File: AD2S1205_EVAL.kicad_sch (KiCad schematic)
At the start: 8 parts, among them U1 AD2S1205, Y1 Crystal

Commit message: Driver schematic done
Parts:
- added C4: 100n, Capacitor_SMD:C_0805_2012Metric_Pad1.18x1.45mm_HandSolder, symbol Device:C
- added C5, C9: 1u, Capacitor_SMD:C_0805_2012Metric_Pad1.18x1.45mm_HandSolder, symbol Device:C
- added C6, C8: DNP, Capacitor_SMD:C_0805_2012Metric_Pad1.18x1.45mm_HandSolder, symbol Device:C
- added C7: C, Capacitor_SMD:C_0805_2012Metric_Pad1.18x1.45mm_HandSolder, symbol Device:C
- added D1, D2, D3, D4: 1N4148, Diode_THT:D_DO-35_SOD27_P7.62mm_Horizontal, symbol Diode:1N4148
- added J1: SIN, Connector_PinHeader_2.54mm:PinHeader_1x02_P2.54mm_Vertical, symbol Connector:Conn_01x02_Pin
- added J2: Power, Connector_PinHeader_2.54mm:PinHeader_1x03_P2.54mm_Vertical, symbol Connector:Conn_01x03_Pin
- added J3: Interface, Connector_PinHeader_2.54mm:PinHeader_1x06_P2.54mm_Vertical, symbol Connector:Conn_01x06_Pin
- added J4: COS, Connector_PinHeader_2.54mm:PinHeader_1x02_P2.54mm_Vertical, symbol Connector:Conn_01x02_Pin
- added J5: DEBUG, symbol Connector:Conn_01x07_Pin
- added Q1, Q3: BD135, Package_TO_SOT_THT:TO-126-3_Vertical, symbol Transistor_BJT:BD135
- added Q2, Q4: BD136, Package_TO_SOT_THT:TO-126-3_Vertical, symbol Transistor_BJT:BD136
- added R10, R11: 22k, Resistor_SMD:R_0805_2012Metric, symbol Device:R
- added R12, R13, R5, R7: 2.2k, Resistor_SMD:R_0805_2012Metric, symbol Device:R
- added R4, R6, R8, R9: 10k, Resistor_SMD:R_0805_2012Metric, symbol Device:R
- added U2: LM358, Package_SO:SO-8_3.9x4.9mm_P1.27mm, symbol Amplifier_Operational:LM358
- C1: footprint (none) -> Capacitor_SMD:C_0805_2012Metric_Pad1.18x1.45mm_HandSolder
- C2, C3: value C -> DNP; footprint (none) -> Capacitor_SMD:C_0805_2012Metric_Pad1.18x1.45mm_HandSolder
- R1, R2: value R -> 68k; footprint (none) -> Resistor_SMD:R_0805_2012Metric
- R3: footprint (none) -> Resistor_SMD:R_0805_2012Metric
- Y1: footprint (none) -> Crystal:Crystal_HC49-U_Vertical
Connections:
- net +5V: now also U1.1 (DVDD), U1.17 (DVDD), U1.39 (AVdd), C4.1, C5.1, C9.1, R10.2
- net GND: now also U1.3 (~{CS}), U1.6 (~{SOE}), C4.2, C5.2, C7.2, C9.2, J3.6 (Pin_6), J5.7 (Pin_7), Q2.1 (E), Q4.1 (E), R11.1, R13.2, R7.2, U2.4 (V-)
- net ~{RD}: now reaches U1.2 (~{RD})
- net ~{RD}: now also J3.1 (Pin_1)
- net at U1.25 (A): now also J5.1 (Pin_1)
- net at U1.26 (B): now also J5.2 (Pin_2)
- net at U1.27 (NM): now also J5.3 (Pin_3)
- net at U1.28 (DIR): now also J5.4 (Pin_4)
- net at U1.29 (DOS): now also J5.5 (Pin_5)
- net at U1.30 (LOT): now also J5.6 (Pin_6)
- net EXC: now reaches U1.34 (EXC)
- net EXC: now also R9.1
- net ~{EXC}: now reaches U1.35 (~{EXC})
- net ~{EXC}: now also R4.1
- net at R1.1, U1.37 (Sin): now also J1.2 (Pin_2)
- net at R1.2, U1.38 (SinLO): now also J1.1 (Pin_1)
- net ~{SAMPLE}: now reaches U1.4 (~{SAMPLE})
- net ~{SAMPLE}: now also J3.2 (Pin_2)
- net at R2.1, U1.40 (CosLO): now also J4.2 (Pin_2)
- net at R2.2, U1.41 (Cos): now also J4.1 (Pin_1)
- net ~{RDVEL}: now reaches U1.5 (~{RDVEL})
- net ~{RDVEL}: now also J3.3 (Pin_3)
- net SO: now reaches U1.7 (DB11/SO)
- net SO: now also J3.5 (Pin_5)
- net SCLK: now reaches U1.8 (DB10)
- net SCLK: now also J3.4 (Pin_4)
- new net: D2.2 (A), Q1.3 (B), R5.2
- new net: D4.1 (K), Q4.3 (B), R13.1
- new net: D3.1 (K), D4.2 (A), U2.1
- new net: D3.2 (A), Q3.3 (B), R12.2
- new net: C8.1, R4.2, R6.1, U2.2 (-)
- new net: C8.2, Q3.1 (E), Q4.2 (C), R6.2
- new net: D1.1 (K), Q2.3 (B), R7.1
- new net: D1.2 (A), D2.1 (K), U2.7
- new net: C6.2, Q1.1 (E), Q2.2 (C), R8.2
- new net: C6.1, R8.1, R9.2, U2.6 (-)
- new net +12V: C7.1, Q1.2 (C), Q3.2 (C), R12.1, R5.1, U2.8 (V+)
- new net 2.5V: R10.1, R11.2, U2.3 (+), U2.5 (+)
- no-connect marks 0 -> 14
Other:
- moved on the sheet: C1, R1, R2, R3

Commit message: Layout
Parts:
- added J6: EXC, Connector_PinHeader_2.54mm:PinHeader_1x02_P2.54mm_Vertical, symbol Connector:Conn_01x02_Pin
- C1: value C -> 1u
- C7: value C -> 100n
- D1, D2, D3, D4: footprint Diode_THT:D_DO-35_SOD27_P7.62mm_Horizontal -> Diode_SMD:D_SMA_Handsoldering
- J5: footprint (none) -> Connector_PinHeader_2.54mm:PinHeader_1x07_P2.54mm_Vertical
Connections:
- net +12V: now also J2.1 (Pin_1)
- net +5V: now also J2.2 (Pin_2)
- net GND: now also J2.3 (Pin_3), J3.4 (Pin_4), Q2.2 (C), Q4.2 (C); no longer J3.6 (Pin_6), Q2.1 (E), Q4.1 (E)
- net SCLK: now also J3.6 (Pin_6); no longer J3.4 (Pin_4)
- net ~{EXC_AMP}: now reaches C8.2, Q3.1 (E), R6.2
- net ~{EXC_AMP}: now also Q4.1 (E), J6.1 (Pin_1); no longer Q4.2 (C)
- net EXC_AMP: now reaches C6.2, Q1.1 (E), R8.2
- net EXC_AMP: now also Q2.1 (E), J6.2 (Pin_2); no longer Q2.2 (C)
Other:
- moved on the sheet: J2

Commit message: layout complete
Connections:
- net +5V: now also J2.3 (Pin_3); no longer J2.2 (Pin_2)
- net GND: now also J2.2 (Pin_2); no longer J2.3 (Pin_3)
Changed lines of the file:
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@@
+    (stroke (width 0) (type default))
+  )
+  (wire (pts (xy 22.86 24.13) (xy 30.48 24.13))
     (stroke (width 0) (type default))
   )
@@
     (stroke (width 0) (type default))
   )
+  (wire (pts (xy 22.86 21.59) (xy 25.4 21.59))
+    (stroke (width 0) (type default))
+  )
   (wire (pts (xy 215.9 60.96) (xy 218.44 60.96))
     (stroke (width 0) (type default))
@@
     (stroke (width 0) (type default))
   )
-  (wire (pts (xy 25.4 24.13) (xy 22.86 24.13))
-    (stroke (width 0) (type default))
-  )
   (wire (pts (xy 218.44 60.96) (xy 223.52 60.96))
     (stroke (width 0) (type default))
@@
     (stroke (width 0) (type default))
   )
-  (wire (pts (xy 25.4 26.67) (xy 25.4 24.13))
+  (wire (pts (xy 25.4 21.59) (xy 25.4 26.67))
     (stroke (width 0) (type default))
   )
@@
   )
   (wire (pts (xy 257.81 38.1) (xy 257.81 45.72))
-    (stroke (width 0) (type default))
-  )
-  (wire (pts (xy 30.48 21.59) (xy 22.86 21.59))
     (stroke (width 0) (type default))
   )
@@
     )
   )
-  (symbol (lib_id "power:+5V") (at 30.48 21.59 0) (unit 1)
-    (in_bom yes) (on_board yes) (dnp no) (fields_autoplaced)
-    (property "Reference" "#PWR025" (at 30.48 25.4 0)
-      (effects (font (size 1.27 1.27)) hide)
-    )
-    (property "Value" "+5V" (at 30.48 17.78 0)
-      (effects (font (size 1.27 1.27)))
-    )
-    (property "Footprint" "" (at 30.48 21.59 0)
-      (effects (font (size 1.27 1.27)) hide)
-    )
-    (property "Datasheet" "" (at 30.48 21.59 0)
-      (effects (font (size 1.27 1.27)) hide)
-    )
+  (symbol (lib_id "power:+5V") (at 30.48 24.13 0) (unit 1)
+    (in_bom yes) (on_board yes) (dnp no) (fields_autoplaced)
+    (property "Reference" "#PWR025" (at 30.48 27.94 0)
+      (effects (font (size 1.27 1.27)) hide)
+    )
+    (property "Value" "+5V" (at 30.48 20.32 0)
+      (effects (font (size 1.27 1.27)))
+    )
+    (property "Footprint" "" (at 30.48 24.13 0)
+      (effects (font (size 1.27 1.27)) hide)
+    )
+    (property "Datasheet" "" (at 30.48 24.13 0)
+      (effects (font (size 1.27 1.27)) hide)
+    )

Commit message: layout complete
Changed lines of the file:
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@@
-    (stroke (width 0) (type default))
-  )
-  (wire (pts (xy 44.45 104.14) (xy 46.99 104.14))
     (stroke (width 0) (type default))
   )

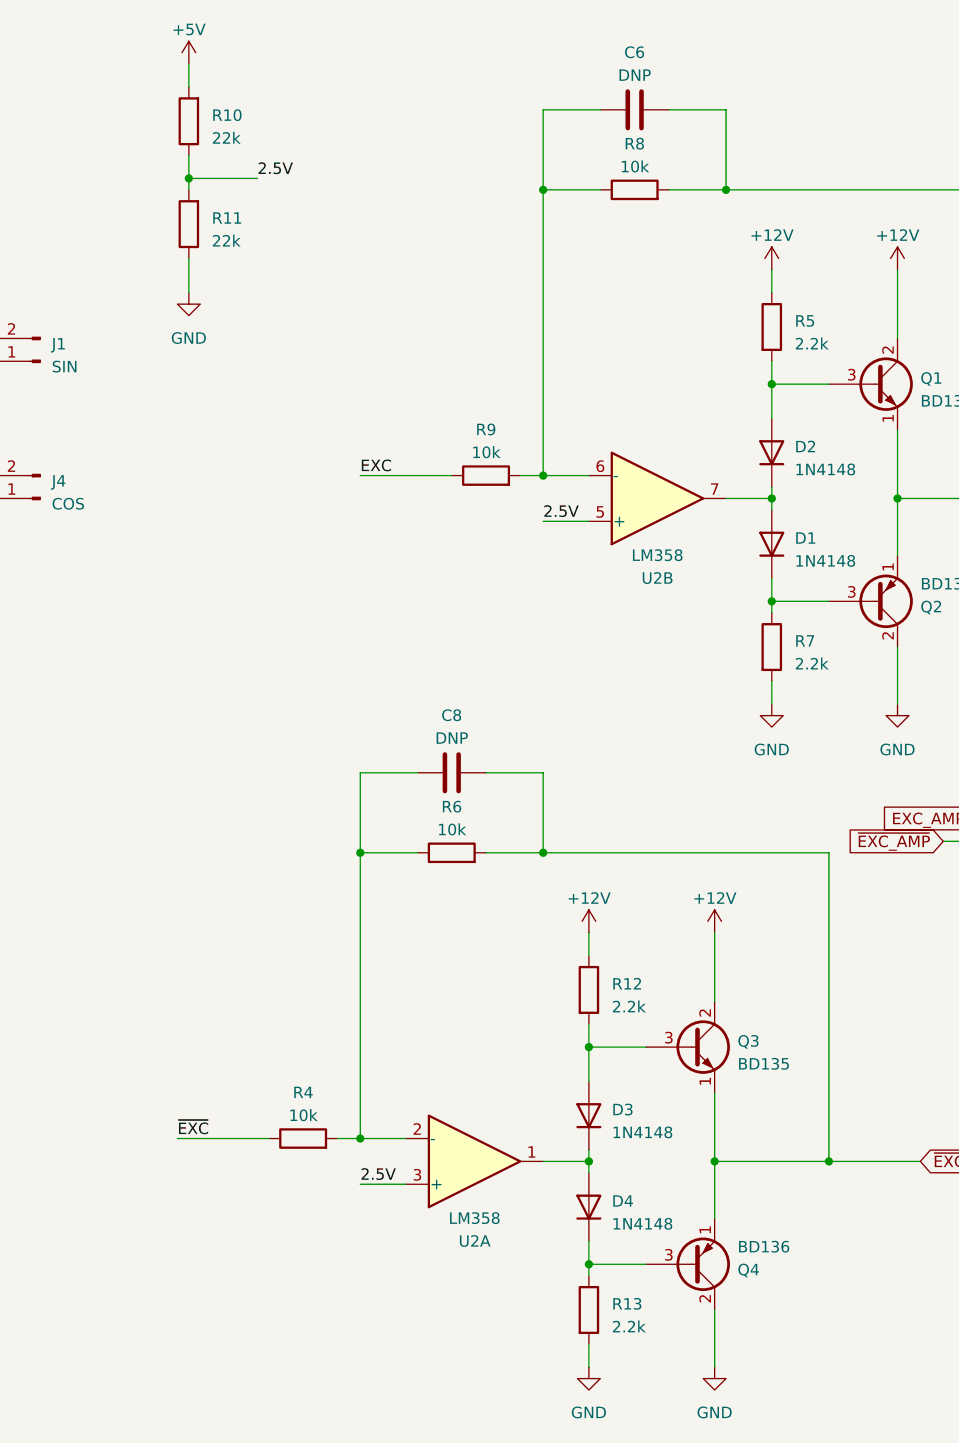
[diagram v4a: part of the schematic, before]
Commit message: Middle point repaired, added crossover dist resistors
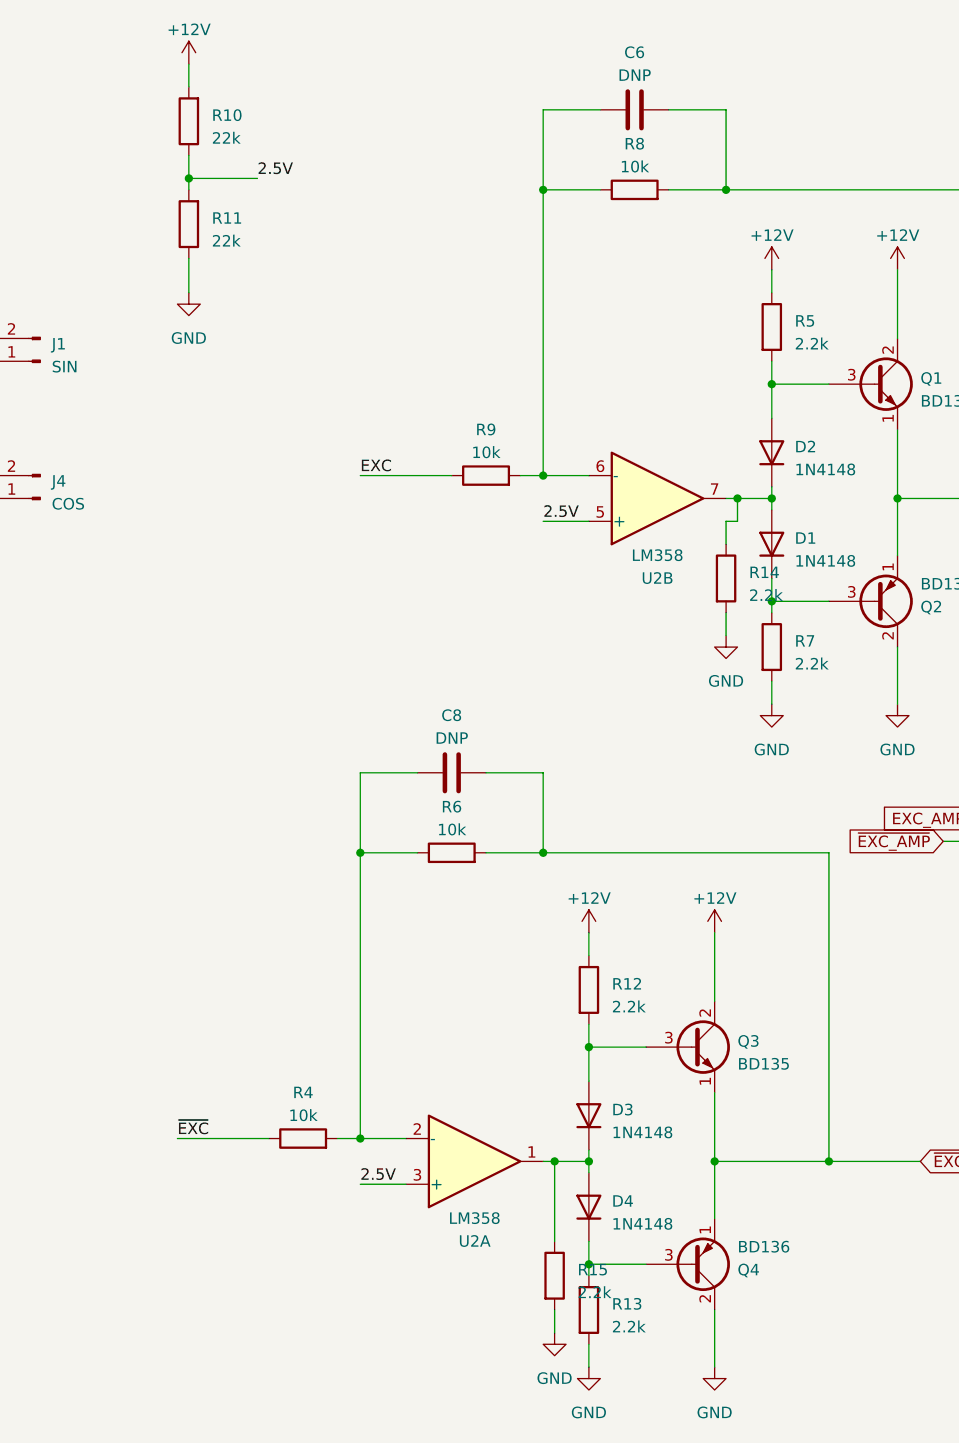
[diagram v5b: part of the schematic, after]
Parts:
- added R14, R15: 2.2k, Resistor_SMD:R_0805_2012Metric, symbol Device:R
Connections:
- net +12V: now also R10.2
- net +5V: no longer R10.2
- net GND: now also R14.2, R15.2
- net at D3.1 (K), D4.2 (A), U2.1: now also R15.1
- net at D1.2 (A), D2.1 (K), U2.7: now also R14.1
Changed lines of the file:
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@@
   (junction (at 223.52 137.16) (diameter 0) (color 0 0 0 0)
   )
+  (junction (at 219.71 137.16) (diameter 0) (color 0 0 0 0)
+  )
   (junction (at 243.84 50.8) (diameter 0) (color 0 0 0 0)
   )
@@
   )
   (junction (at 97.79 30.48) (diameter 0) (color 0 0 0 0)
+  )
+  (junction (at 240.03 63.5) (diameter 0) (color 0 0 0 0)
   )
   (junction (at 67.31 19.05) (diameter 0) (color 0 0 0 0)
@@
     (stroke (width 0) (type default))
   )
-  (wire (pts (xy 218.44 137.16) (xy 223.52 137.16))
+  (wire (pts (xy 218.44 137.16) (xy 219.71 137.16))
     (stroke (width 0) (type default))
   )
@@
     (stroke (width 0) (type default))
   )
+  (wire (pts (xy 219.71 137.16) (xy 223.52 137.16))
+    (stroke (width 0) (type default))
+  )
   (wire (pts (xy 198.12 102.87) (xy 204.47 102.87))
     (stroke (width 0) (type default))
@@
     (stroke (width 0) (type default))
   )
+  (wire (pts (xy 240.03 63.5) (xy 243.84 63.5))
+    (stroke (width 0) (type default))
+  )
+  (wire (pts (xy 219.71 156.21) (xy 219.71 153.67))
+    (stroke (width 0) (type default))
+  )
   (wire (pts (xy 93.98 107.95) (xy 93.98 110.49))
     (stroke (width 0) (type default))
   )
+  (wire (pts (xy 219.71 137.16) (xy 219.71 146.05))
+    (stroke (width 0) (type default))
+  )
   (wire (pts (xy 243.84 83.82) (xy 243.84 86.36))
     (stroke (width 0) (type default))
@@
     (stroke (width 0) (type default))
   )
-  (wire (pts (xy 238.76 63.5) (xy 243.84 63.5))
+  (wire (pts (xy 238.76 63.5) (xy 240.03 63.5))
     (stroke (width 0) (type default))
   )
@@
     (stroke (width 0) (type default))
   )
+  (wire (pts (xy 238.76 66.04) (xy 240.03 66.04))
+    (stroke (width 0) (type default))
+  )
   (wire (pts (xy 96.52 107.95) (xy 96.52 110.49))
     (stroke (width 0) (type default))
@@
     (stroke (width 0) (type default))
   )
+  (wire (pts (xy 240.03 66.04) (xy 240.03 63.5))
+    (stroke (width 0) (type default))
+  )
   (wire (pts (xy 25.4 59.69) (xy 25.4 58.42))
     (stroke (width 0) (type default))
@@
     (stroke (width 0) (type default))
   )
+  (wire (pts (xy 238.76 78.74) (xy 238.76 76.2))
+    (stroke (width 0) (type default))
+  )
   (wire (pts (xy 157.48 48.26) (xy 152.4 48.26))
     (stroke (width 0) (type default))
@@
   )
   (wire (pts (xy 26.67 19.05) (xy 22.86 19.05))
+    (stroke (width 0) (type default))
+  )
+  (wire (pts (xy 238.76 68.58) (xy 238.76 66.04))
     (stroke (width 0) (type default))
   )
@@
         (path "/32cdb66b-76ff-43dd-bd7a-d5b9ef172269"
           (reference "R5") (unit 1)
+        )
+      )
+    )
+  )
+  (symbol (lib_id "Device:R") (at 238.76 72.39 0) (unit 1)
+    (in_bom yes) (on_board yes) (dnp no) (fields_autoplaced)
+    (property "Reference" "R14" (at 241.3 71.755 0)
+      (effects (font (size 1.27 1.27)) (justify left))
+    )
+    (property "Value" "2.2k" (at 241.3 74.295 0)
+      (effects (font (size 1.27 1.27)) (justify left))
+    )
+    (property "Footprint" "Resistor_SMD:R_0805_2012Metric" (at 236.982 72.39 90)
+      (effects (font (size 1.27 1.27)) hide)
+    )
+    (property "Datasheet" "~" (at 238.76 72.39 0)
+      (effects (font (size 1.27 1.27)) hide)
+    )
+    (pin "1")
+    (pin "2")
+    (instances
+      (project "AD2S1205_EVAL"
+        (path "/32cdb66b-76ff-43dd-bd7a-d5b9ef172269"
+          (reference "R14") (unit 1)
         )
       )
@@
         (path "/32cdb66b-76ff-43dd-bd7a-d5b9ef172269"
           (reference "J5") (unit 1)
+        )
+      )
+    )
+  )
+  (symbol (lib_id "power:GND") (at 238.76 78.74 0) (unit 1)
+    (in_bom yes) (on_board yes) (dnp no) (fields_autoplaced)
+    (property "Reference" "#PWR028" (at 238.76 85.09 0)
+      (effects (font (size 1.27 1.27)) hide)
+    )
+    (property "Value" "GND" (at 238.76 83.82 0)
+      (effects (font (size 1.27 1.27)))
+    )
+    (property "Footprint" "" (at 238.76 78.74 0)
+      (effects (font (size 1.27 1.27)) hide)
+    )
+    (property "Datasheet" "" (at 238.76 78.74 0)
+      (effects (font (size 1.27 1.27)) hide)
+    )
+    (pin "1")
+    (instances
+      (project "AD2S1205_EVAL"
+        (path "/32cdb66b-76ff-43dd-bd7a-d5b9ef172269"
+          (reference "#PWR028") (unit 1)
         )
       )
@@
     )
   )
+  (symbol (lib_id "Device:R") (at 219.71 149.86 0) (unit 1)
+    (in_bom yes) (on_board yes) (dnp no) (fields_autoplaced)
+    (property "Reference" "R15" (at 222.25 149.225 0)
+      (effects (font (size 1.27 1.27)) (justify left))
+    )
+    (property "Value" "2.2k" (at 222.25 151.765 0)
+      (effects (font (size 1.27 1.27)) (justify left))
+    )
+    (property "Footprint" "Resistor_SMD:R_0805_2012Metric" (at 217.932 149.86 90)
+      (effects (font (size 1.27 1.27)) hide)
+    )
+    (property "Datasheet" "~" (at 219.71 149.86 0)
+      (effects (font (size 1.27 1.27)) hide)
+    )
+    (pin "1")
+    (pin "2")
+    (instances
+      (project "AD2S1205_EVAL"
+        (path "/32cdb66b-76ff-43dd-bd7a-d5b9ef172269"
+          (reference "R15") (unit 1)
+        )
+      )
+    )
+  )
   (symbol (lib_id "Device:C") (at 67.31 24.13 0) (unit 1)
     (in_bom yes) (on_board yes) (dnp no) (fields_autoplaced)
@@
     )
   )
-  (symbol (lib_id "power:+5V") (at 179.07 15.24 0) (unit 1)
+  (symbol (lib_id "power:GND") (at 243.84 86.36 0) (unit 1)
+    (in_bom yes) (on_board yes) (dnp no) (fields_autoplaced)
+    (property "Reference" "#PWR013" (at 243.84 92.71 0)
+      (effects (font (size 1.27 1.27)) hide)
+    )
+    (property "Value" "GND" (at 243.84 91.44 0)
+      (effects (font (size 1.27 1.27)))
+    )
+    (property "Footprint" "" (at 243.84 86.36 0)
+      (effects (font (size 1.27 1.27)) hide)
+    )
+    (property "Datasheet" "" (at 243.84 86.36 0)
+      (effects (font (size 1.27 1.27)) hide)
+    )
+    (pin "1")
+    (instances
+      (project "AD2S1205_EVAL"
+        (path "/32cdb66b-76ff-43dd-bd7a-d5b9ef172269"
+          (reference "#PWR013") (unit 1)
+        )
+      )
+    )
+  )
+  (symbol (lib_id "power:+12V") (at 179.07 15.24 0) (unit 1)
     (in_bom yes) (on_board yes) (dnp no) (fields_autoplaced)
     (property "Reference" "#PWR016" (at 179.07 19.05 0)
       (effects (font (size 1.27 1.27)) hide)
     )
-    (property "Value" "+5V" (at 179.07 11.43 0)
+    (property "Value" "+12V" (at 179.07 11.43 0)
       (effects (font (size 1.27 1.27)))
     )
@@
     )
   )
-  (symbol (lib_id "power:GND") (at 243.84 86.36 0) (unit 1)
-    (in_bom yes) (on_board yes) (dnp no) (fields_autoplaced)
-    (property "Reference" "#PWR013" (at 243.84 92.71 0)
-      (effects (font (size 1.27 1.27)) hide)
-    )
-    (property "Value" "GND" (at 243.84 91.44 0)
-      (effects (font (size 1.27 1.27)))
-    )
-    (property "Footprint" "" (at 243.84 86.36 0)
-      (effects (font (size 1.27 1.27)) hide)
-    )
-    (property "Datasheet" "" (at 243.84 86.36 0)
-      (effects (font (size 1.27 1.27)) hide)
-    )
-    (pin "1")
-    (instances
-      (project "AD2S1205_EVAL"
-        (path "/32cdb66b-76ff-43dd-bd7a-d5b9ef172269"
-          (reference "#PWR013") (unit 1)
-        )
-      )
+  (symbol (lib_id "power:GND") (at 219.71 156.21 0) (unit 1)
+    (in_bom yes) (on_board yes) (dnp no) (fields_autoplaced)
+    (property "Reference" "#PWR029" (at 219.71 162.56 0)
+      (effects (font (size 1.27 1.27)) hide)
+    )
+    (property "Value" "GND" (at 219.71 161.29 0)
+      (effects (font (size 1.27 1.27)))
+    )
+    (property "Footprint" "" (at 219.71 156.21 0)
+      (effects (font (size 1.27 1.27)) hide)
+    )
+    (property "Datasheet" "" (at 219.71 156.21 0)
+      (effects (font (size 1.27 1.27)) hide)
+    )
+    (pin "1")
+    (instances
+      (project "AD2S1205_EVAL"
+        (path "/32cdb66b-76ff-43dd-bd7a-d5b9ef172269"
+          (reference "#PWR029") (unit 1)
+        )
+      )
